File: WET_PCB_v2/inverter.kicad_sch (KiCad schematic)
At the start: 36 parts, among them Q1 IRF530NPBF, Q2 IRF530NPBF, Q3 IRF530NPBF, Q4 IRF530NPBF, U3 IR2110, U4 IR2110

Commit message: most routing done. to do: 12v routing, test points, deco, checking clearance
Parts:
- D7: footprint Diode_THT:D_A-405_P2.54mm_Vertical_CathodeUp -> Diode_THT:D_A-405_P7.62mm_Horizontal
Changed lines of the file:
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@@
 			)
 		)
-		(property "Footprint" "Diode_THT:D_A-405_P2.54mm_Vertical_CathodeUp"
+		(property "Footprint" "Diode_THT:D_A-405_P7.62mm_Horizontal"
 			(at 207.01 51.435 0)
 			(hide yes)

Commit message: labels
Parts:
- C10, C8, C9: value B32529C1104K000 -> C_inv_out
- C11: value C -> C_inv_out
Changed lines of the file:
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@@
 			)
 		)
-		(property "Value" "B32529C1104K000"
+		(property "Value" "C_inv_out"
 			(at 147.32 62.23 0)
 			(hide yes)
@@
 			)
 		)
-		(property "Value" "B32529C1104K000"
+		(property "Value" "C_inv_out"
 			(at 147.32 69.85 0)
 			(hide yes)
@@
 			)
 		)
-		(property "Value" "B32529C1104K000"
+		(property "Value" "C_inv_out"
 			(at 147.32 77.47 0)
 			(hide yes)
@@
 			)
 		)
-		(property "Value" "C"
+		(property "Value" "C_inv_out"
 			(at 147.32 48.26 90)
 			(hide yes)

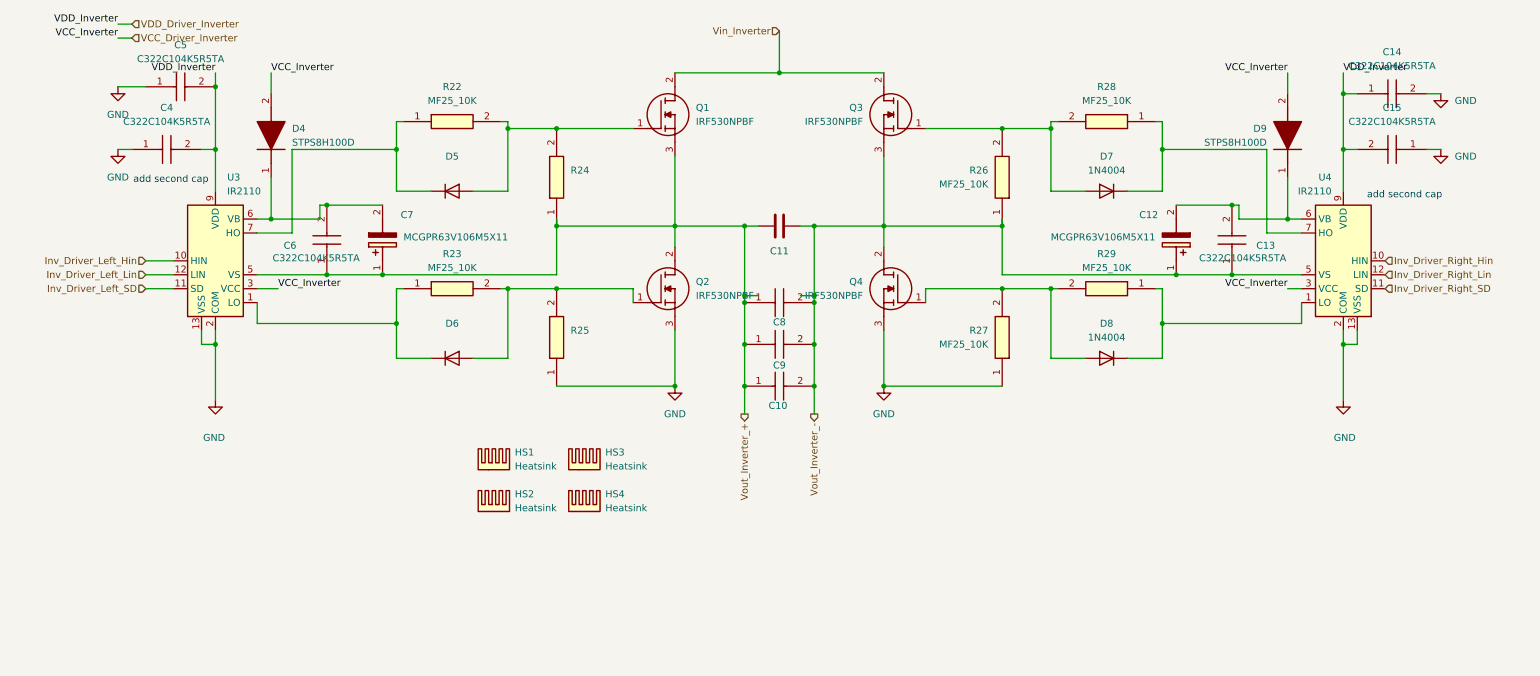
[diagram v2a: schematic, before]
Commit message: some caps were missing and wrong way around AAAAAAAAAAAAAAAAAAAAAAAAAAAAAAAAAAA
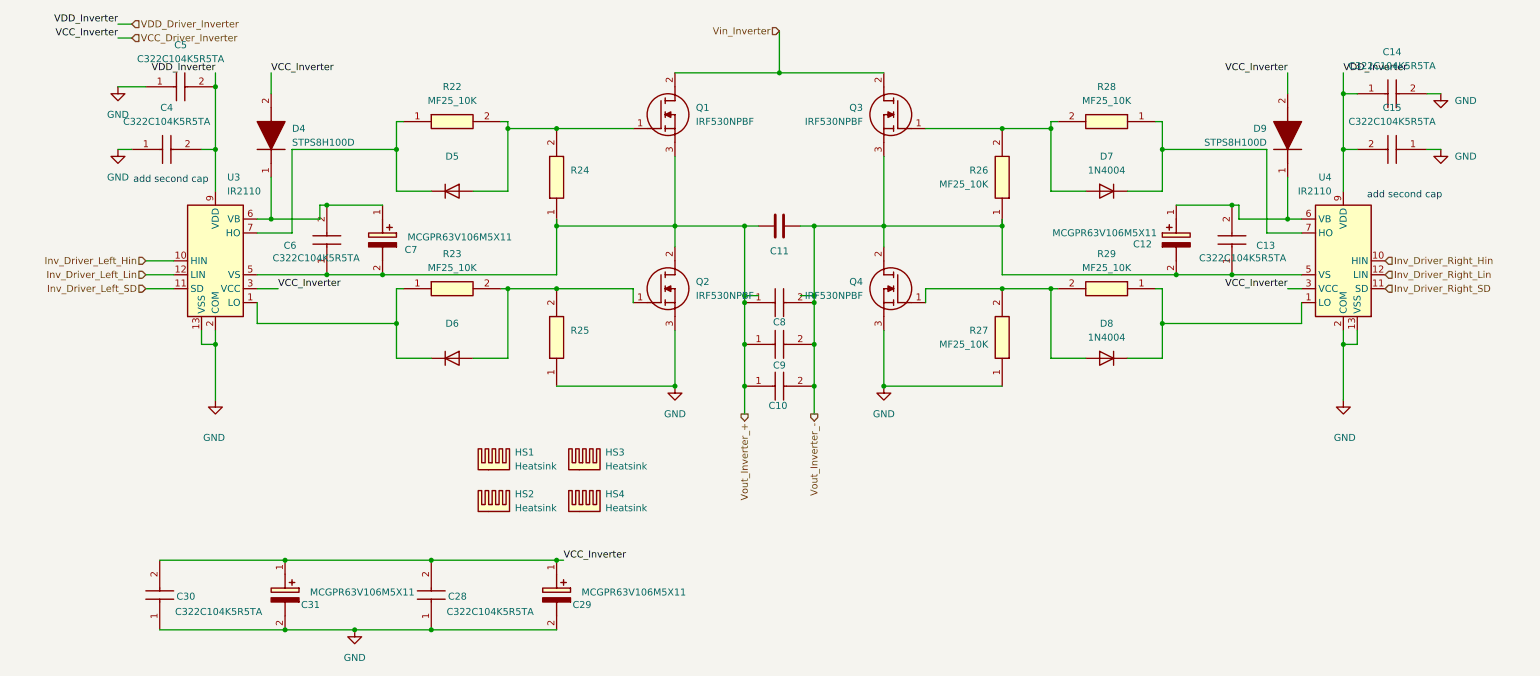
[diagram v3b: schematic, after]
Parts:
- added C28, C30: C322C104K5R5TA, Capacitor_THT:C_Disc_D4.3mm_W1.9mm_P5.00mm, symbol C322C104K5R5TA:C322C104K5R5TA
- added C29, C31: MCGPR63V106M5X11, Capacitor_THT:C_Radial_D5.0mm_H11.0mm_P2.00mm, symbol MCGPR63V106M5X11:MCGPR63V106M5X11
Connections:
- net GND: now also C28.1, C29.2 (-), C30.1, C31.2 (-)
- net VCC_Driver_Inverter: now also C28.2, C29.1 (+), C30.2, C31.1 (+)
- net Vout_Inverter_+: now also C7.2 (-); no longer C7.1 (+)
- net Vout_Inverter_-: now also C12.2 (-); no longer C12.1 (+)
- net at C13.2, D9.1 (K), U4.6 (VB): now also C12.1 (+); no longer C12.2 (-)
- net at C6.2, D4.1 (K), U3.6 (VB): now also C7.1 (+); no longer C7.2 (-)

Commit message: imma hand it in now
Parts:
- removed C10: C_inv_out, Inductor_THT:L_Axial_L23.4mm_D12.7mm_P32.00mm_Horizontal_Vishay_IHA-203, symbol B32529C1104K000:B32529C1104K000
- removed C11: C_inv_out, Capacitor_THT:C_Rect_L32.0mm_W15.0mm_P27.00mm, symbol Device:C
- removed C8: C_inv_out, Capacitor_THT:C_Rect_L7.0mm_W2.5mm_P5.00mm, symbol B32529C1104K000:B32529C1104K000
- removed C9: C_inv_out, Capacitor_THT:C_Rect_L24.0mm_W12.8mm_P22.50mm_MKT, symbol B32529C1104K000:B32529C1104K000

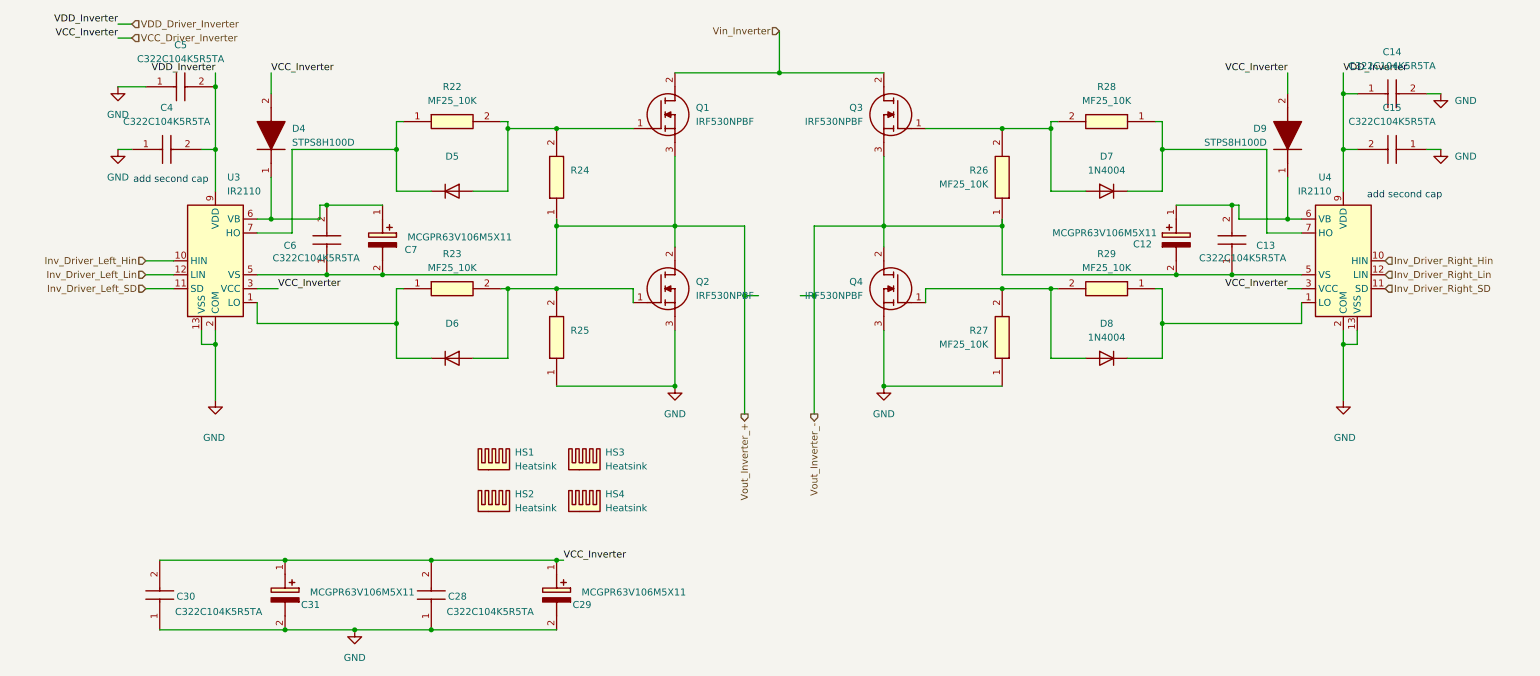
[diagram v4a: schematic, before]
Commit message: added values and notes for assembly
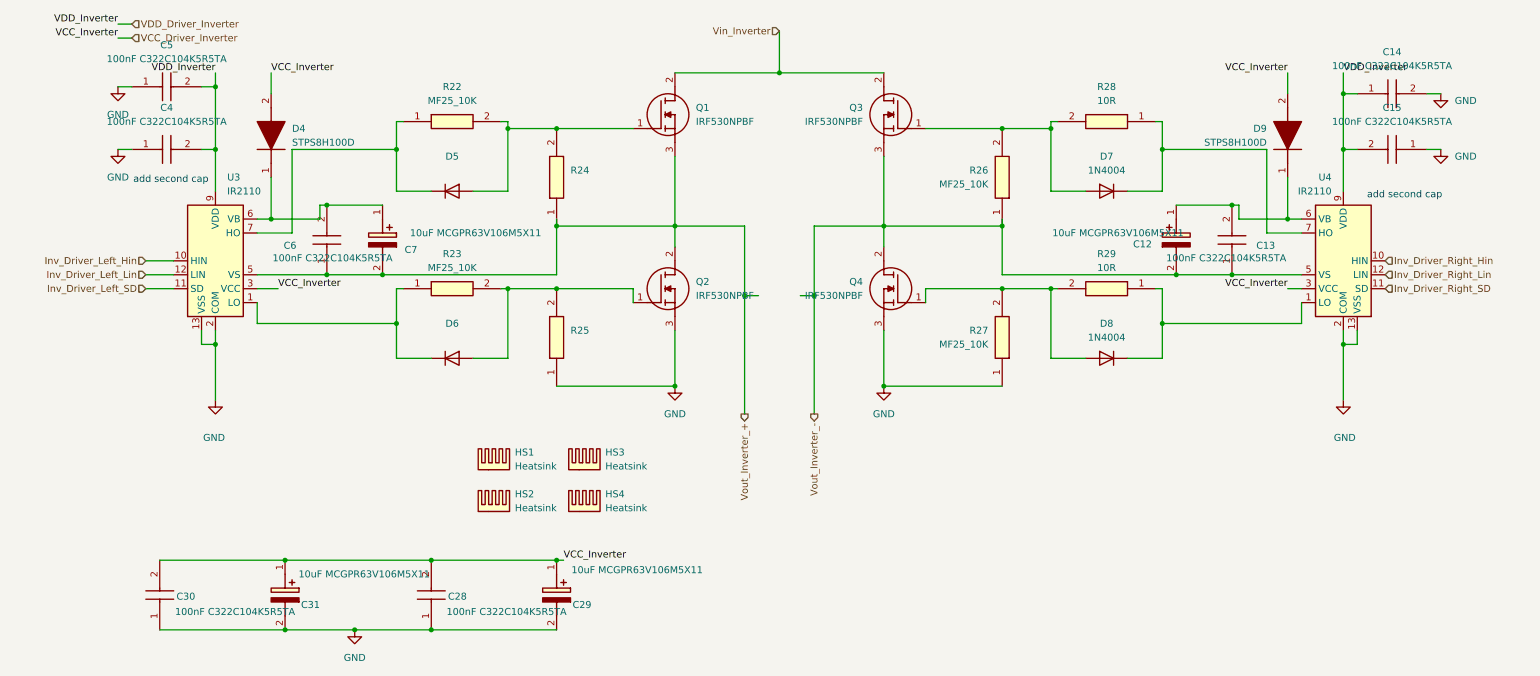
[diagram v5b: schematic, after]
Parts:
- C12, C29, C31, C7: value MCGPR63V106M5X11 -> 10uF MCGPR63V106M5X11
- C13, C14, C15, C28, C30, C4, C5, C6: value C322C104K5R5TA -> 100nF C322C104K5R5TA
- R25: value MF25_10K -> 10K
- R28, R29: value MF25_10K -> 10R
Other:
- moved on the sheet: C5
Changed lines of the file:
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@@
 	)
 	(junction
-		(at 44.45 27.94)
-		(diameter 0)
-		(color 0 0 0 0)
-	)
-	(junction
 		(at 106.68 53.34)
 		(diameter 0)
@@
 	)
 	(junction
+		(at 44.45 27.94)
+		(diameter 0)
+		(color 0 0 0 0)
+	)
+	(junction
 		(at 140.97 66.04)
 		(diameter 0)
@@
 	(wire
 		(pts
+			(xy 41.91 27.94) (xy 44.45 27.94)
+		)
+		(stroke
+			(width 0)
+			(type default)
+		)
+	)
+	(wire
+		(pts
 			(xy 54.61 25.4) (xy 54.61 29.21)
 		)
@@
 	(wire
 		(pts
-			(xy 26.67 27.94) (xy 31.75 27.94)
+			(xy 26.67 27.94) (xy 29.21 27.94)
 		)
 		(stroke
@@
 			)
 		)
-		(property "Value" "MF25_10K"
+		(property "Value" "10R"
 			(at 207.01 60.96 0)
 			(show_name no)
@@
 			)
 		)
-		(property "Value" "C322C104K5R5TA"
+		(property "Value" "100nF C322C104K5R5TA"
 			(at 239.776 59.182 90)
 			(show_name no)
@@
 			)
 		)
-		(property "Value" "C322C104K5R5TA"
+		(property "Value" "100nF C322C104K5R5TA"
 			(at 86.614 123.698 90)
 			(show_name no)
@@
 			)
 		)
-		(property "Value" "C322C104K5R5TA"
+		(property "Value" "100nF C322C104K5R5TA"
 			(at 37.084 123.698 90)
 			(show_name no)
@@
 			)
 		)
-		(property "Value" "C322C104K5R5TA"
+		(property "Value" "100nF C322C104K5R5TA"
 			(at 259.08 24.13 0)
 			(show_name no)
@@
 			)
 		)
-		(property "Value" "MF25_10K"
+		(property "Value" "10K"
 			(at 109.22 74.9299 90)
 			(hide yes)
@@
 			)
 		)
-		(property "Value" "MCGPR63V106M5X11"
-			(at 80.772 120.142 90)
+		(property "Value" "10uF MCGPR63V106M5X11"
+			(at 83.566 116.84 90)
 			(show_name no)
 			(do_not_autoplace no)
@@
 			)
 		)
-		(property "Value" "C322C104K5R5TA"
+		(property "Value" "100nF C322C104K5R5TA"
 			(at 259.08 34.29 0)
 			(show_name no)
@@
 	(symbol
 		(lib_id "C322C104K5R5TA:C322C104K5R5TA")
-		(at 31.75 27.94 0)
+		(at 29.21 27.94 0)
 		(unit 1)
 		(body_style 1)
@@
 		(fields_autoplaced yes)
 		(property "Reference" "C5"
-			(at 38.1 20.32 0)
+			(at 35.56 20.32 0)
 			(show_name no)
 			(do_not_autoplace no)
@@
 			)
 		)
-		(property "Value" "C322C104K5R5TA"
-			(at 38.1 22.86 0)
+		(property "Value" "100nF C322C104K5R5TA"
+			(at 35.56 22.86 0)
 			(show_name no)
 			(do_not_autoplace no)
@@
 		)
 		(property "Footprint" "Capacitor_THT:C_Disc_D4.3mm_W1.9mm_P5.00mm"
-			(at 40.64 124.13 0)
+			(at 38.1 124.13 0)
 			(hide yes)
 			(show_name no)
@@
 		)
 		(property "Datasheet" "https://www.yageogroup.com/content/datasheet/asset/file/KEM_C1050_GOLDMAX_X7R"
-			(at 40.64 224.13 0)
+			(at 38.1 224.13 0)
 			(hide yes)
 			(show_name no)
@@
 		)
 		(property "Description" "GoldMax, Commercial Standard"
-			(at 31.75 27.94 0)
+			(at 29.21 27.94 0)
 			(hide yes)
 			(show_name no)
@@
 		)
 		(property "Height" "6.6"
-			(at 40.64 424.13 0)
+			(at 38.1 424.13 0)
 			(hide yes)
 			(show_name no)
@@
 		)
 		(property "Farnell Part Number" ""
-			(at 40.64 524.13 0)
+			(at 38.1 524.13 0)
 			(hide yes)
 			(show_name no)
@@
 		)
 		(property "Farnell Price/Stock" ""
-			(at 40.64 624.13 0)
+			(at 38.1 624.13 0)
 			(hide yes)
 			(show_name no)
@@
 		)
 		(property "Manufacturer_Name" "Yageo Group"
-			(at 40.64 724.13 0)
+			(at 38.1 724.13 0)
 			(hide yes)
 			(show_name no)
@@
 		)
 		(property "Manufacturer_Part_Number" "C322C104K5R5TA"
-			(at 40.64 824.13 0)
+			(at 38.1 824.13 0)
 			(hide yes)
 			(show_name no)
@@
 			)
 		)
-		(property "Value" "C322C104K5R5TA"
+		(property "Value" "100nF C322C104K5R5TA"
 			(at 35.56 34.29 0)
 			(show_name no)
@@
 			)
 		)
-		(property "Value" "C322C104K5R5TA"
+		(property "Value" "100nF C322C104K5R5TA"
 			(at 54.864 59.182 90)
 			(show_name no)
@@
 			)
 		)
-		(property "Value" "MCGPR63V106M5X11"
-			(at 130.302 120.142 90)
+		(property "Value" "10uF MCGPR63V106M5X11"
+			(at 133.35 116.078 90)
 			(show_name no)
 			(do_not_autoplace no)
@@
 			)
 		)
-		(property "Value" "MCGPR63V106M5X11"
+		(property "Value" "10uF MCGPR63V106M5X11"
 			(at 197.104 54.61 90)
 			(show_name no)
@@
 			)
 		)
-		(property "Value" "MF25_10K"
+		(property "Value" "10R"
 			(at 207.01 30.48 0)
 			(show_name no)
@@
 			)
 		)
-		(property "Value" "MCGPR63V106M5X11"
-			(at 98.552 55.372 90)
+		(property "Value" "10uF MCGPR63V106M5X11"
+			(at 103.886 54.61 90)
 			(show_name no)
 			(do_not_autoplace no)
